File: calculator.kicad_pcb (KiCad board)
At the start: 2 copper layers, 2 parts, among them J1 NHD-0216CW-AB3, U1 STM32F103RETx

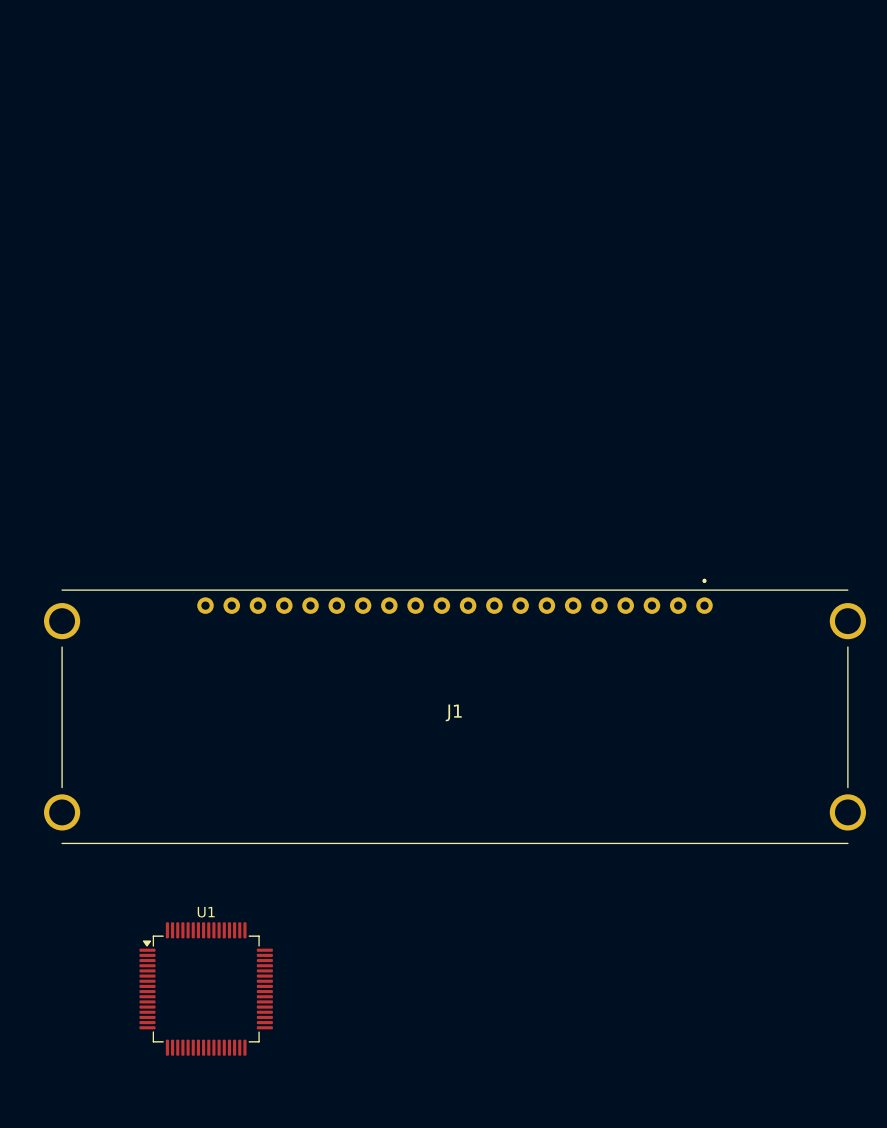
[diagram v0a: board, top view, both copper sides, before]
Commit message: Finish schematic design
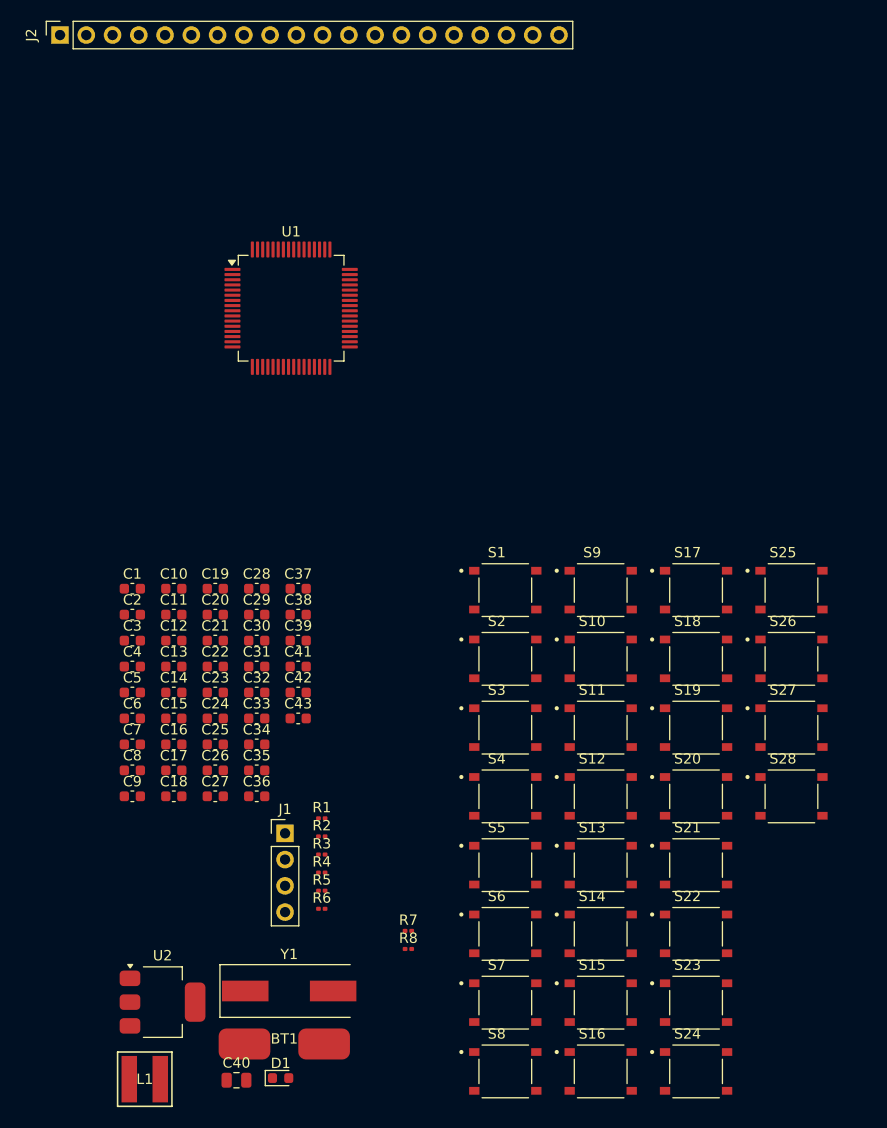
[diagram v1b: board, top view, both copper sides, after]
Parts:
- added BT1: Battery, Battery_Pads:Battery_Pads, F.Cu at (149.7, 115.9)
- added C1: 100nF, Capacitor_SMD:C_0603_1608Metric, F.Cu at (135.0, 71.8)
- added C10: 100nF, Capacitor_SMD:C_0603_1608Metric, F.Cu at (139.0, 71.8)
- added C11: 100nF, Capacitor_SMD:C_0603_1608Metric, F.Cu at (139.0, 74.3)
- added C12: 100nF, Capacitor_SMD:C_0603_1608Metric, F.Cu at (139.0, 76.9)
- added C13: 100nF, Capacitor_SMD:C_0603_1608Metric, F.Cu at (139.0, 79.4)
- added C14: 100nF, Capacitor_SMD:C_0603_1608Metric, F.Cu at (139.0, 81.9)
- added C15: 100nF, Capacitor_SMD:C_0603_1608Metric, F.Cu at (139.0, 84.4)
- added C16: 100nF, Capacitor_SMD:C_0603_1608Metric, F.Cu at (139.0, 86.9)
- added C17: 100nF, Capacitor_SMD:C_0603_1608Metric, F.Cu at (139.0, 89.4)
- added C18: 100nF, Capacitor_SMD:C_0603_1608Metric, F.Cu at (139.0, 91.9)
- added C19: 100nF, Capacitor_SMD:C_0603_1608Metric, F.Cu at (143.0, 71.8)
- added C2: 100nF, Capacitor_SMD:C_0603_1608Metric, F.Cu at (135.0, 74.3)
- added C20: 100nF, Capacitor_SMD:C_0603_1608Metric, F.Cu at (143.0, 74.3)
- added C21: 100nF, Capacitor_SMD:C_0603_1608Metric, F.Cu at (143.0, 76.9)
- added C22: 100nF, Capacitor_SMD:C_0603_1608Metric, F.Cu at (143.0, 79.4)
- added C23: 100nF, Capacitor_SMD:C_0603_1608Metric, F.Cu at (143.0, 81.9)
- added C24: 100nF, Capacitor_SMD:C_0603_1608Metric, F.Cu at (143.0, 84.4)
- added C25: 100nF, Capacitor_SMD:C_0603_1608Metric, F.Cu at (143.0, 86.9)
- added C26: 100nF, Capacitor_SMD:C_0603_1608Metric, F.Cu at (143.0, 89.4)
- added C27: 100nF, Capacitor_SMD:C_0603_1608Metric, F.Cu at (143.0, 91.9)
- added C28: 100nF, Capacitor_SMD:C_0603_1608Metric, F.Cu at (147.0, 71.8)
- added C29: 100nF, Capacitor_SMD:C_0603_1608Metric, F.Cu at (147.0, 74.3)
- added C3: 100nF, Capacitor_SMD:C_0603_1608Metric, F.Cu at (135.0, 76.9)
- added C30: 100nF, Capacitor_SMD:C_0603_1608Metric, F.Cu at (147.0, 76.9)
- added C31: 100nF, Capacitor_SMD:C_0603_1608Metric, F.Cu at (147.0, 79.4)
- added C32: 100nF, Capacitor_SMD:C_0603_1608Metric, F.Cu at (147.0, 81.9)
- added C33: 100nF, Capacitor_SMD:C_0603_1608Metric, F.Cu at (147.0, 84.4)
- added C34: 100nF, Capacitor_SMD:C_0603_1608Metric, F.Cu at (147.0, 86.9)
- added C35: 100nF, Capacitor_SMD:C_0603_1608Metric, F.Cu at (147.0, 89.4)
- added C36: 100nF, Capacitor_SMD:C_0603_1608Metric, F.Cu at (147.0, 91.9)
- added C37: 100nF, Capacitor_SMD:C_0603_1608Metric, F.Cu at (151.1, 71.8)
- added C38: 100nF, Capacitor_SMD:C_0603_1608Metric, F.Cu at (151.1, 74.3)
- added C39: 2.2uF, Capacitor_SMD:C_0603_1608Metric, F.Cu at (151.1, 76.9)
- added C4: 100nF, Capacitor_SMD:C_0603_1608Metric, F.Cu at (135.0, 79.4)
- added C40: 47uF, Capacitor_SMD:C_0805_2012Metric, F.Cu at (145.1, 119.4)
- added C41: 10uF, Capacitor_SMD:C_0603_1608Metric, F.Cu at (151.1, 79.4)
- added C42: 1uF, Capacitor_SMD:C_0603_1608Metric, F.Cu at (151.1, 81.9)
- added C43: 10nF, Capacitor_SMD:C_0603_1608Metric, F.Cu at (151.1, 84.4)
- added C5: 100nF, Capacitor_SMD:C_0603_1608Metric, F.Cu at (135.0, 81.9)
- added C6: 100nF, Capacitor_SMD:C_0603_1608Metric, F.Cu at (135.0, 84.4)
- added C7: 20pF, Capacitor_SMD:C_0603_1608Metric, F.Cu at (135.0, 86.9)
- added C8: 20pF, Capacitor_SMD:C_0603_1608Metric, F.Cu at (135.0, 89.4)
- added C9: 100nF, Capacitor_SMD:C_0603_1608Metric, F.Cu at (135.0, 91.9)
- added D1: LED, LED_SMD:LED_0603_1608Metric, F.Cu at (149.4, 119.2)
- added J2: Conn_01x20_Socket, Connector_PinSocket_2.54mm:PinSocket_1x20_P2.54mm_Vertical, F.Cu at (128.0, 18.3)
- added L1: 6.8uH, IND_NP-4R7NC_SUM:IND_NP-4R7NC_SUM, F.Cu at (136.2, 119.3)
- added R1: R, Resistor_SMD:R_0201_0603Metric, F.Cu at (153.3, 94.0)
- added R2: R, Resistor_SMD:R_0201_0603Metric, F.Cu at (153.3, 95.8)
- added R3: R, Resistor_SMD:R_0201_0603Metric, F.Cu at (153.3, 97.5)
- added R4: R, Resistor_SMD:R_0201_0603Metric, F.Cu at (153.3, 99.3)
- added R5: R, Resistor_SMD:R_0201_0603Metric, F.Cu at (153.3, 101.0)
- added R6: R, Resistor_SMD:R_0201_0603Metric, F.Cu at (153.3, 102.8)
- added R7: 10K, Resistor_SMD:R_0201_0603Metric, F.Cu at (161.7, 104.9)
- added R8: 10K, Resistor_SMD:R_0201_0603Metric, F.Cu at (161.7, 106.7)
- added S1: TS-1187A-B-A-B, TS-1187A-B-A-B:SW_TS-1187A-B-A-B, F.Cu at (171.1, 72.0)
- added S10: TS-1187A-B-A-B, TS-1187A-B-A-B:SW_TS-1187A-B-A-B, F.Cu at (180.3, 78.6)
- added S11: TS-1187A-B-A-B, TS-1187A-B-A-B:SW_TS-1187A-B-A-B, F.Cu at (180.3, 85.3)
- added S12: TS-1187A-B-A-B, TS-1187A-B-A-B:SW_TS-1187A-B-A-B, F.Cu at (180.3, 91.9)
- added S13: TS-1187A-B-A-B, TS-1187A-B-A-B:SW_TS-1187A-B-A-B, F.Cu at (180.3, 98.6)
- added S14: TS-1187A-B-A-B, TS-1187A-B-A-B:SW_TS-1187A-B-A-B, F.Cu at (180.3, 105.2)
- added S15: TS-1187A-B-A-B, TS-1187A-B-A-B:SW_TS-1187A-B-A-B, F.Cu at (180.3, 111.9)
- added S16: TS-1187A-B-A-B, TS-1187A-B-A-B:SW_TS-1187A-B-A-B, F.Cu at (180.3, 118.5)
- added S17: TS-1187A-B-A-B, TS-1187A-B-A-B:SW_TS-1187A-B-A-B, F.Cu at (189.5, 72.0)
- added S18: TS-1187A-B-A-B, TS-1187A-B-A-B:SW_TS-1187A-B-A-B, F.Cu at (189.5, 78.6)
- added S19: TS-1187A-B-A-B, TS-1187A-B-A-B:SW_TS-1187A-B-A-B, F.Cu at (189.5, 85.3)
- added S2: TS-1187A-B-A-B, TS-1187A-B-A-B:SW_TS-1187A-B-A-B, F.Cu at (171.1, 78.6)
- added S20: TS-1187A-B-A-B, TS-1187A-B-A-B:SW_TS-1187A-B-A-B, F.Cu at (189.5, 91.9)
- added S21: TS-1187A-B-A-B, TS-1187A-B-A-B:SW_TS-1187A-B-A-B, F.Cu at (189.5, 98.6)
- added S22: TS-1187A-B-A-B, TS-1187A-B-A-B:SW_TS-1187A-B-A-B, F.Cu at (189.5, 105.2)
- added S23: TS-1187A-B-A-B, TS-1187A-B-A-B:SW_TS-1187A-B-A-B, F.Cu at (189.5, 111.9)
- added S24: TS-1187A-B-A-B, TS-1187A-B-A-B:SW_TS-1187A-B-A-B, F.Cu at (189.5, 118.5)
- added S25: TS-1187A-B-A-B, TS-1187A-B-A-B:SW_TS-1187A-B-A-B, F.Cu at (198.8, 72.0)
- added S26: TS-1187A-B-A-B, TS-1187A-B-A-B:SW_TS-1187A-B-A-B, F.Cu at (198.8, 78.6)
- added S27: TS-1187A-B-A-B, TS-1187A-B-A-B:SW_TS-1187A-B-A-B, F.Cu at (198.8, 85.3)
- added S28: TS-1187A-B-A-B, TS-1187A-B-A-B:SW_TS-1187A-B-A-B, F.Cu at (198.8, 91.9)
- added S3: TS-1187A-B-A-B, TS-1187A-B-A-B:SW_TS-1187A-B-A-B, F.Cu at (171.1, 85.3)
- added S4: TS-1187A-B-A-B, TS-1187A-B-A-B:SW_TS-1187A-B-A-B, F.Cu at (171.1, 91.9)
- added S5: TS-1187A-B-A-B, TS-1187A-B-A-B:SW_TS-1187A-B-A-B, F.Cu at (171.1, 98.6)
- added S6: TS-1187A-B-A-B, TS-1187A-B-A-B:SW_TS-1187A-B-A-B, F.Cu at (171.1, 105.2)
- added S7: TS-1187A-B-A-B, TS-1187A-B-A-B:SW_TS-1187A-B-A-B, F.Cu at (171.1, 111.9)
- added S8: TS-1187A-B-A-B, TS-1187A-B-A-B:SW_TS-1187A-B-A-B, F.Cu at (171.1, 118.5)
- added S9: TS-1187A-B-A-B, TS-1187A-B-A-B:SW_TS-1187A-B-A-B, F.Cu at (180.3, 72.0)
- added U2: AMS1117, Package_TO_SOT_SMD:SOT-223-3_TabPin2, F.Cu at (137.9, 111.8)
- added Y1: 8Mhz, Crystal:Crystal_SMD_HC49-SD, F.Cu at (150.2, 110.7)
- J1: value NHD-0216CW-AB3 -> Conn_01x04_Pin; footprint NHD0216CWAB3:NHD0216CWAB3 -> Connector_PinHeader_2.54mm:PinHeader_1x04_P2.54mm_Vertical
- moved U1 66.4 mm to (150.4, 44.7)
- moved J1 24.3 mm to (149.8, 95.5)
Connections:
- J1 pad 1: unconnected-(J1-VSS_1-Pad1) -> GND
- J1 pad 2: unconnected-(J1-VDD-Pad2) -> SWDCLK
- J1 pad 3: unconnected-(J1-REGVDD-Pad3) -> SWDIO
- J1 pad 4: unconnected-(J1-D/C-Pad4) -> +5V
- U1 pad 10: unconnected-(U1-PC2-Pad10) -> COL_3
- U1 pad 11: unconnected-(U1-PC3-Pad11) -> ROW_1
- U1 pad 13: unconnected-(U1-VDDA-Pad13) -> Net-(U1-VDDA)
- U1 pad 24: unconnected-(U1-PC4-Pad24) -> ROW_2
- U1 pad 25: unconnected-(U1-PC5-Pad25) -> ROW_3
- U1 pad 37: unconnected-(U1-PC6-Pad37) -> ROW_4
- U1 pad 38: unconnected-(U1-PC7-Pad38) -> ROW_5
- U1 pad 39: unconnected-(U1-PC8-Pad39) -> ROW_6
- U1 pad 40: unconnected-(U1-PC9-Pad40) -> ROW_7
- U1 pad 46: unconnected-(U1-PA13-Pad46) -> SWDIO
- U1 pad 49: unconnected-(U1-PA14-Pad49) -> SWDCLK
- U1 pad 5: unconnected-(U1-PD0-Pad5) -> OSC_IN
- U1 pad 51: unconnected-(U1-PC10-Pad51) -> ROW_8
- U1 pad 52: unconnected-(U1-PC11-Pad52) -> ROW_9
- U1 pad 55: unconnected-(U1-PB3-Pad55) -> OLED_RES
- U1 pad 56: unconnected-(U1-PB4-Pad56) -> OLED_SA0
- U1 pad 58: unconnected-(U1-PB6-Pad58) -> OLED_SCL
- U1 pad 59: unconnected-(U1-PB7-Pad59) -> OLED_SDA
- U1 pad 6: unconnected-(U1-PD1-Pad6) -> OSC_OUT
- U1 pad 60: unconnected-(U1-BOOT0-Pad60) -> Net-(U1-BOOT0)
- U1 pad 7: unconnected-(U1-NRST-Pad7) -> NRST
- U1 pad 8: unconnected-(U1-PC0-Pad8) -> COL_1
- U1 pad 9: unconnected-(U1-PC1-Pad9) -> COL_2
